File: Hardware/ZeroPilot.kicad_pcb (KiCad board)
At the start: 4 copper layers, 100 x 50 mm, 223 parts, among them J1 GH-6, J10 GH-4, J11 GH-3, J12 GH-4, J13 GH-2, J14 GH-4, J15 GH-4, J16 GH-4, J17 GH-4, J18 GH-6, J19 GH-6, J2 GH-6, J20 GH-6, J21 GH-6, J22 GH-6, J23 GH-6, J3 GH-6, J4 GH-6, J5 GH-6, J6 GH-6, J7 SPOX-2, J8 Micro_SD_Card, J9 USB_MICRO_B, Q1 Q_PMOS_DGS, Q2 Q_NMOS_GSD, U1 TPS54308, U10 STM32F030RCT6, U11 M24C64-WDW6TP, U12 ICM-20602, U13 MS5637-02BA03, U14 FT4232H, U2 TPS54308DDCT, U8 MCP1826S-3302E/DB, U9 STM32F765ZGT6, Y1 32.768kHz, Y2 8MHz, Y3 32.768kHz, Y4 8MHz, Y5 Crystal_GND24

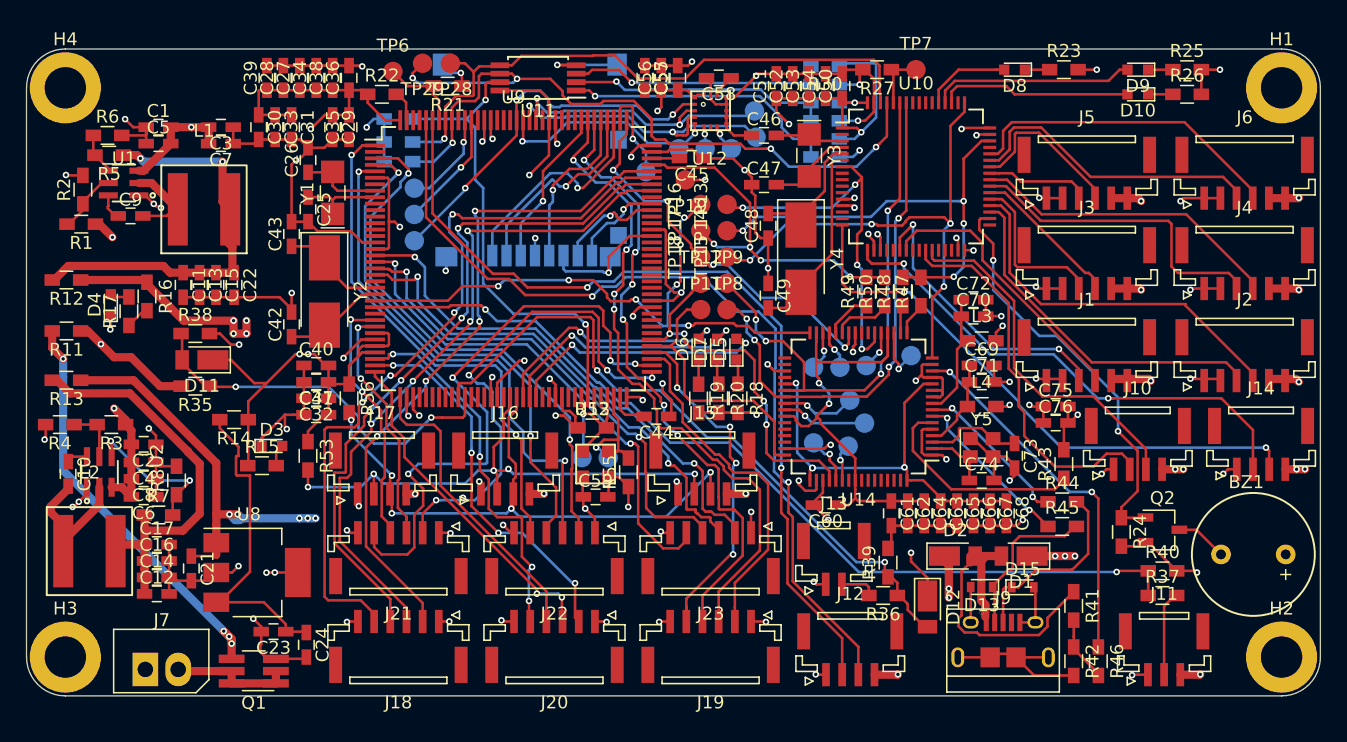
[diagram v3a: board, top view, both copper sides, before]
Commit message: Updated Footprints
Updated the footprints to 5.1, added 3D models to all components.
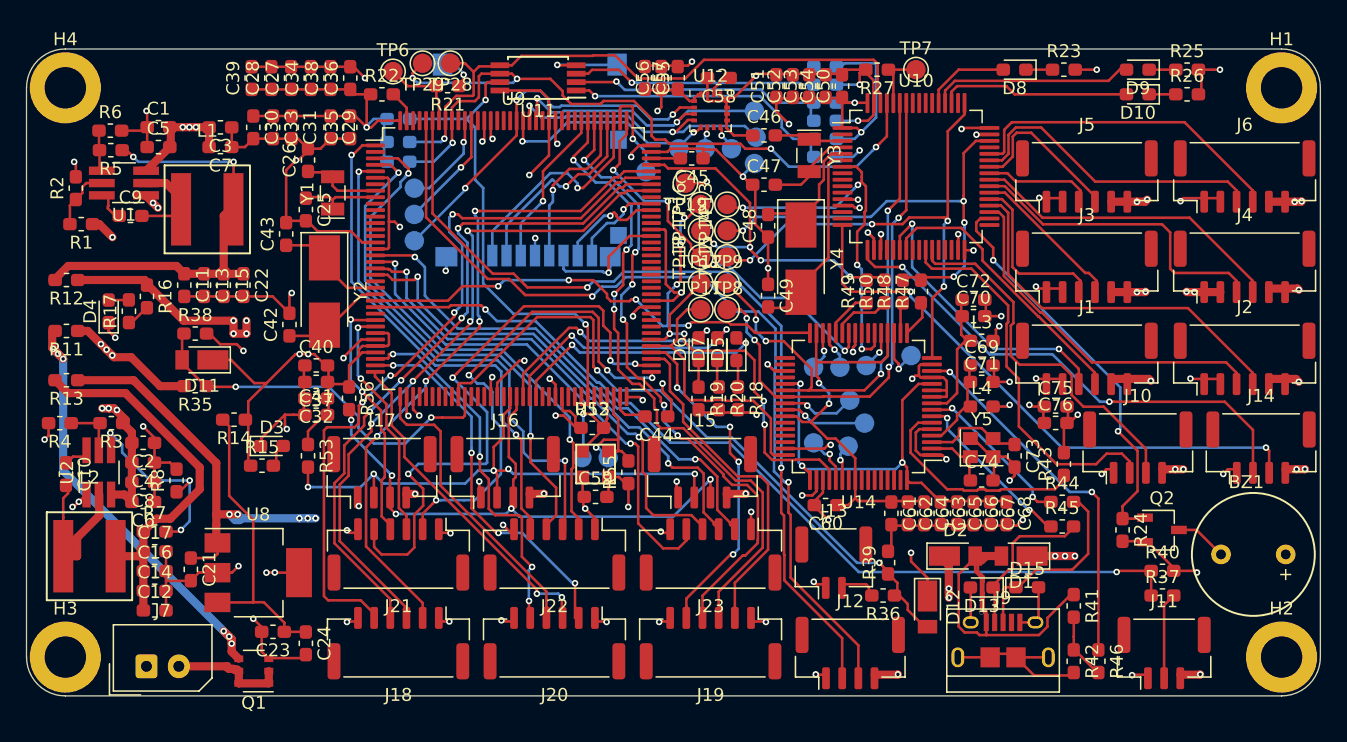
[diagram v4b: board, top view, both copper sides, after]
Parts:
- added TP10: GND_TST, TestPoint:TestPoint_Pad_D1.5mm, B.Cu at (106.3, 108.9)
- C1, C10, C11, C12, C13, C14, C15, C16, C17, C2, C21, C22, C23, C24, C25, C26, C27, C28, C29, C3, C30, C31, C32, C33, C34, C35, C36, C37, C38, C39, C4, C40, C41, C42, C43, C44, C45, C46, C47, C48, C49, C5, C50, C51, C52, C53, C54, C55, C56, C57, C58, C59, C6, C60, C61, C62, C63, C64, C65, C66, C67, C68, C69, C7, C70, C71, C72, C73, C74, C75, C76, C8, C9: footprint Capacitors_SMD:C_0603_HandSoldering -> Capacitor_SMD:C_0603_1608Metric_Pad1.05x0.95mm_HandSolder
- D1, D11, D12, D2: footprint Diodes_SMD:D_PowerDI-123 -> Diode_SMD:D_PowerDI-123
- D10, D3, D4, D5, D6, D7, D8, D9: footprint LEDs:LED_0603 -> LED_SMD:LED_0603_1608Metric_Pad1.05x0.95mm_HandSolder
- D13, D15: footprint Diodes_SMD:D_0603 -> Diode_SMD:D_0603_1608Metric_Pad1.05x0.95mm_HandSolder
- H1, H2, H3, H4: footprint Mounting_Holes:MountingHole_3.2mm_M3_ISO14580_Pad -> MountingHole:MountingHole_3.2mm_M3_ISO14580_Pad
- J1, J18, J19, J2, J20, J21, J22, J23, J3, J4, J5, J6: footprint Connectors_JST:JST_GH_BM06B-GHS-TBT_06x1.25mm_Straight -> Connector_JST:JST_GH_BM06B-GHS-TBT_1x06-1MP_P1.25mm_Vertical
- J10, J12, J14, J15, J16, J17: footprint Connectors_JST:JST_GH_BM04B-GHS-TBT_04x1.25mm_Straight -> Connector_JST:JST_GH_BM04B-GHS-TBT_1x04-1MP_P1.25mm_Vertical
- J11: footprint Connectors_JST:JST_GH_BM03B-GHS-TBT_03x1.25mm_Straight -> Connector_JST:JST_GH_BM03B-GHS-TBT_1x03-1MP_P1.25mm_Vertical
- J13: footprint Connectors_JST:JST_GH_BM02B-GHS-TBT_02x1.25mm_Straight -> Connector_JST:JST_GH_BM02B-GHS-TBT_1x02-1MP_P1.25mm_Vertical
- J7: footprint Connectors_Molex:Molex_SPOX-5267_22-03-5025_02x2.54mm_Straight -> Connector_Molex:Molex_SPOX_5267-02A_1x02_P2.50mm_Vertical
- L3, L4: footprint Inductors_SMD:L_0603_HandSoldering -> Inductor_SMD:L_0603_1608Metric_Pad1.05x0.95mm_HandSolder
- Q1: footprint WARG:TSOT-23-6_MK06A_HandSoldering -> WARG-kicad:IRF5806
- Q2: footprint TO_SOT_Packages_SMD:TSOT-23 -> Package_TO_SOT_SMD:TSOT-23
- R1, R11, R12, R13, R14, R15, R16, R17, R18, R19, R2, R20, R21, R22, R23, R24, R25, R26, R27, R28, R29, R3, R30, R31, R32, R33, R34, R35, R36, R37, R38, R39, R4, R40, R41, R42, R43, R44, R45, R46, R47, R48, R49, R5, R50, R51, R52, R53, R54, R55, R56, R6, R7, R8: footprint Resistors_SMD:R_0603_HandSoldering -> Resistor_SMD:R_0603_1608Metric_Pad1.05x0.95mm_HandSolder
- TP1, TP11, TP12, TP13, TP14, TP15, TP16, TP17, TP18, TP19, TP2, TP20, TP21, TP22, TP23, TP24, TP25, TP26, TP27, TP28, TP29, TP3, TP30, TP31, TP32, TP33, TP34, TP35, TP4, TP5, TP6, TP7, TP8, TP9: footprint Measurement_Points:Measurement_Point_Round-SMD-Pad_Small -> TestPoint:TestPoint_Pad_D1.5mm
- U1, U2: footprint WARG:TPS54308DDCT -> Package_TO_SOT_SMD:TSOT-23-6_HandSoldering
- U10, U14: footprint Housings_QFP:LQFP-64_10x10mm_Pitch0.5mm -> Package_QFP:LQFP-64_10x10mm_P0.5mm
- U11: footprint Housings_SSOP:TSSOP-8_4.4x3mm_Pitch0.65mm -> Package_SO:TSSOP-8_4.4x3mm_P0.65mm
- U12: footprint WARG:ICM-20602 -> Package_LGA:LGA-16_3x3mm_P0.5mm
- U13: footprint WARG:MS5637-02BA03 -> WARG-kicad:MS5637-02BA03
- U8: footprint TO_SOT_Packages_SMD:SOT-223 -> Package_TO_SOT_SMD:SOT-223
- U9: footprint Housings_QFP:LQFP-144_20x20mm_Pitch0.5mm -> Package_QFP:LQFP-144_20x20mm_P0.5mm
- Y1, Y3: footprint Crystals:Crystal_SMD_MicroCrystal_CC7V-T1A-2pin_3.2x1.5mm_HandSoldering -> Crystal:Crystal_SMD_MicroCrystal_CC7V-T1A-2Pin_3.2x1.5mm
- Y2, Y4: footprint Crystals:Crystal_SMD_5032-2pin_5.0x3.2mm_HandSoldering -> Crystal:Crystal_SMD_5032-2Pin_5.0x3.2mm_HandSoldering
- Y5: footprint Crystals:Crystal_SMD_2520-4pin_2.5x2.0mm -> Crystal:Crystal_SMD_2520-4Pin_2.5x2.0mm
- moved R7 1.32 mm to (59.9, 137.3)
- moved C12 1.29 mm to (59.9, 143.4)
- moved C39 1.18 mm to (67.4, 102.2)
- moved C14 1.04 mm to (59.9, 141.9)
- moved C28 0.93 mm to (68.9, 102.2)
- moved C16 0.79 mm to (59.9, 140.3)
- moved C22 0.72 mm to (66.8, 118.2)
- moved C27 0.67 mm to (70.4, 102.2)
- moved C15 0.60 mm to (65.2, 118.2)
- moved R2 0.56 mm to (53.8, 110.8)
- moved C17 0.55 mm to (59.9, 138.8)
- moved D4 0.55 mm to (56.4, 120.3)
- moved R6 0.43 mm to (56.5, 106.3)
- moved C30 0.42 mm to (67.5, 106.1)
- moved C34 0.42 mm to (72.0, 102.2)
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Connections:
- J9 pad 4: (no net) -> Net-(J9-Pad4)
- U10 pad 10: (no net) -> Net-(U10-Pad10)
- U10 pad 11: (no net) -> Net-(U10-Pad11)
- U10 pad 14: (no net) -> Net-(U10-Pad14)
- U10 pad 15: (no net) -> Net-(U10-Pad15)
- U10 pad 2: (no net) -> Net-(U10-Pad2)
- U10 pad 20: (no net) -> Net-(U10-Pad20)
- U10 pad 21: (no net) -> Net-(U10-Pad21)
- U10 pad 24: (no net) -> Net-(U10-Pad24)
- U10 pad 25: (no net) -> Net-(U10-Pad25)
- U10 pad 28: (no net) -> Net-(U10-Pad28)
- U10 pad 29: (no net) -> Net-(U10-Pad29)
- U10 pad 30: (no net) -> Net-(U10-Pad30)
- U10 pad 33: (no net) -> Net-(U10-Pad33)
- U10 pad 45: (no net) -> Net-(U10-Pad45)
- U10 pad 50: (no net) -> Net-(U10-Pad50)
- U10 pad 54: (no net) -> Net-(U10-Pad54)
- U10 pad 55: (no net) -> Net-(U10-Pad55)
- U10 pad 56: (no net) -> Net-(U10-Pad56)
- U10 pad 57: (no net) -> Net-(U10-Pad57)
- U10 pad 8: (no net) -> Net-(U10-Pad8)
- U10 pad 9: (no net) -> Net-(U10-Pad9)
- U12 pad 7: (no net) -> Net-(U12-Pad7)
- U14 pad 23: (no net) -> Net-(U14-Pad23)
- U14 pad 24: (no net) -> Net-(U14-Pad24)
- U14 pad 33: (no net) -> Net-(U14-Pad33)
- U14 pad 34: (no net) -> Net-(U14-Pad34)
- U14 pad 36: (no net) -> Net-(U14-Pad36)
- U14 pad 43: (no net) -> Net-(U14-Pad43)
- U14 pad 44: (no net) -> Net-(U14-Pad44)
- U14 pad 45: (no net) -> Net-(U14-Pad45)
- U14 pad 46: (no net) -> Net-(U14-Pad46)
- U14 pad 55: (no net) -> Net-(U14-Pad55)
- U14 pad 57: (no net) -> Net-(U14-Pad57)
- U14 pad 58: (no net) -> Net-(U14-Pad58)
- U14 pad 59: (no net) -> Net-(U14-Pad59)
- U14 pad 60: (no net) -> Net-(U14-Pad60)
- U14 pad 61: (no net) -> Net-(U14-Pad61)
- U14 pad 62: (no net) -> Net-(U14-Pad62)
- U14 pad 63: (no net) -> Net-(U14-Pad63)
- U9 pad 10: (no net) -> Net-(U9-Pad10)
- U9 pad 100: (no net) -> Net-(U9-Pad100)
- U9 pad 11: (no net) -> Net-(U9-Pad11)
- U9 pad 117: (no net) -> Net-(U9-Pad117)
- U9 pad 118: (no net) -> Net-(U9-Pad118)
- U9 pad 119: (no net) -> Net-(U9-Pad119)
- U9 pad 12: (no net) -> Net-(U9-Pad12)
- U9 pad 122: (no net) -> Net-(U9-Pad122)
- U9 pad 127: (no net) -> Net-(U9-Pad127)
- U9 pad 128: (no net) -> Net-(U9-Pad128)
- U9 pad 129: (no net) -> Net-(U9-Pad129)
- U9 pad 13: (no net) -> Net-(U9-Pad13)
- U9 pad 132: (no net) -> Net-(U9-Pad132)
- U9 pad 135: (no net) -> Net-(U9-Pad135)
- U9 pad 14: (no net) -> Net-(U9-Pad14)
- U9 pad 141: (no net) -> Net-(U9-Pad141)
- U9 pad 142: (no net) -> Net-(U9-Pad142)
- U9 pad 15: (no net) -> Net-(U9-Pad15)
- U9 pad 2: (no net) -> Net-(U9-Pad2)
- U9 pad 22: (no net) -> Net-(U9-Pad22)
- U9 pad 27: (no net) -> Net-(U9-Pad27)
- U9 pad 40: (no net) -> Net-(U9-Pad40)
- U9 pad 41: (no net) -> Net-(U9-Pad41)
- U9 pad 42: (no net) -> Net-(U9-Pad42)
- U9 pad 43: (no net) -> Net-(U9-Pad43)
- U9 pad 44: (no net) -> Net-(U9-Pad44)
- U9 pad 45: (no net) -> Net-(U9-Pad45)
- U9 pad 48: (no net) -> Net-(U9-Pad48)
- U9 pad 49: (no net) -> Net-(U9-Pad49)
- U9 pad 50: (no net) -> Net-(U9-Pad50)
- U9 pad 53: (no net) -> Net-(U9-Pad53)
- U9 pad 59: (no net) -> Net-(U9-Pad59)
- U9 pad 60: (no net) -> Net-(U9-Pad60)
- U9 pad 63: (no net) -> Net-(U9-Pad63)
- U9 pad 64: (no net) -> Net-(U9-Pad64)
- U9 pad 65: (no net) -> Net-(U9-Pad65)
- U9 pad 67: (no net) -> Net-(U9-Pad67)
- U9 pad 68: (no net) -> Net-(U9-Pad68)
- U9 pad 7: (no net) -> Net-(U9-Pad7)
- U9 pad 79: (no net) -> Net-(U9-Pad79)
- U9 pad 80: (no net) -> Net-(U9-Pad80)
- U9 pad 81: (no net) -> Net-(U9-Pad81)
- U9 pad 82: (no net) -> Net-(U9-Pad82)
- U9 pad 85: (no net) -> Net-(U9-Pad85)
- U9 pad 86: (no net) -> Net-(U9-Pad86)
- U9 pad 87: (no net) -> Net-(U9-Pad87)
- U9 pad 88: (no net) -> Net-(U9-Pad88)
- U9 pad 89: (no net) -> Net-(U9-Pad89)
- U9 pad 90: (no net) -> Net-(U9-Pad90)
- U9 pad 91: (no net) -> Net-(U9-Pad91)
- U9 pad 92: (no net) -> Net-(U9-Pad92)
- U9 pad 93: (no net) -> Net-(U9-Pad93)
- U9 pad 96: (no net) -> Net-(U9-Pad96)
- U9 pad 97: (no net) -> Net-(U9-Pad97)
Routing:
- net GND: track 309.8 -> 322.0 mm, vias 77 -> 78
- net /5V_USB: track 23.8 -> 30.8 mm
- net /POWER/INT_FB: track 11.8 -> 16.2 mm, vias 2 -> 3
- net /POWER/3V3_JMP: track 25.4 -> 23.4 mm
- net /POWER/6V_EXT_JMP: track 31.8 -> 33.4 mm
- net /VBATT: track 29.3 -> 30.8 mm, vias 4 -> 10
- net /POWER/EXT_SW: track 6.76 -> 8.27 mm
- net /POWER/5V_INT_JMP: track 31.3 -> 29.9 mm
- net /POWER/VBATT_JMP: track 32.3 -> 33.6 mm, vias 4 -> 6
- net /6V_EXT: track 37.3 -> 38.5 mm, vias 17 -> 20
- net Net-(C63-Pad1): track 33.5 -> 34.7 mm, vias 4 -> 3
- net /SAFETY_DBG_RX: track 42.5 -> 41.4 mm
- net /3V3: track 177.4 -> 178.5 mm, vias 28 -> 27
- net /RX4: track 48.1 -> 49.2 mm
- net /MISO1: track 23.2 -> 22.2 mm
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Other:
- net class Default: clearance 0.0889 -> 0.127
- rule trace_clearance: 0.0889 -> 0.127

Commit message: HW Bootcamp for Zeropilot R1
Changed the board to R1.
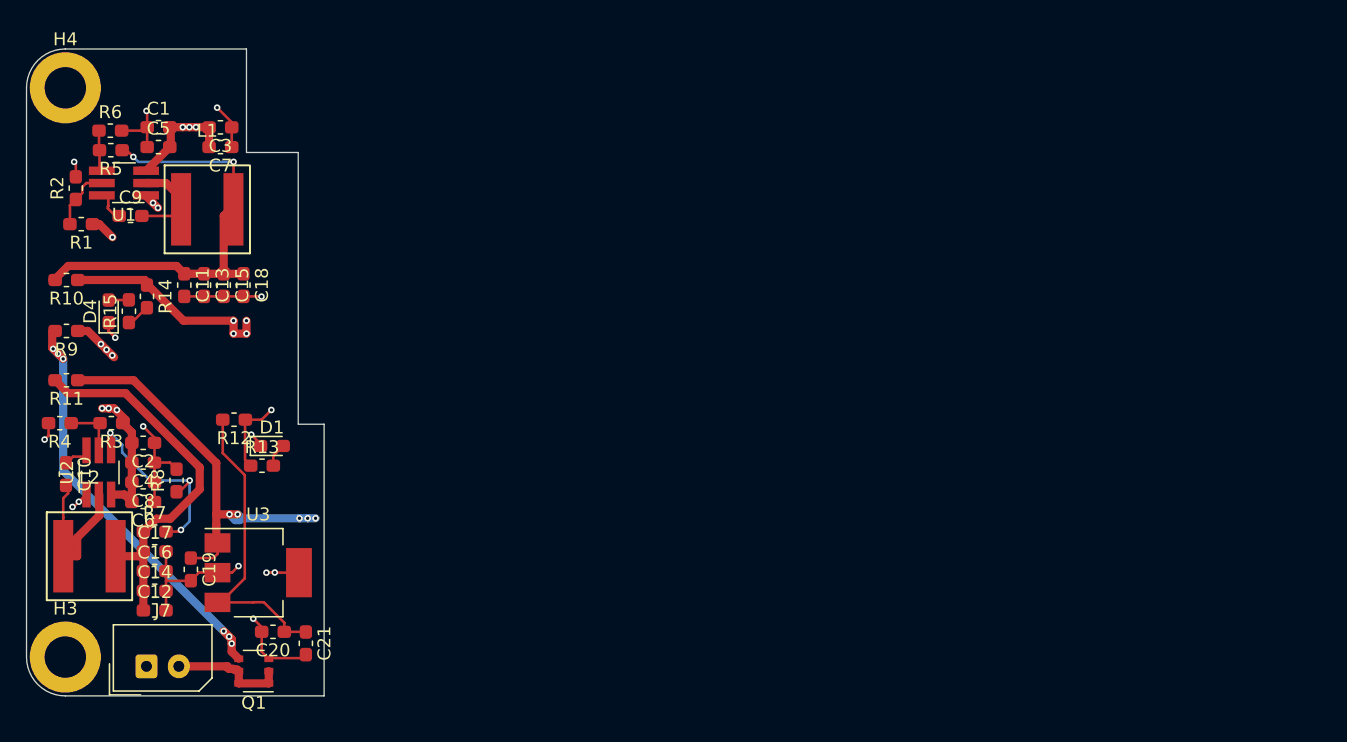
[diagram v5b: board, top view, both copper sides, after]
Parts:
- removed BZ1: Buzzer, WARG:AI-1027-TWT-3V-R
- removed C25, C26, C46, C47: 14pF, Capacitor_SMD:C_0603_1608Metric_Pad1.05x0.95mm_HandSolder
- removed C27, C28, C29, C30, C31, C32, C33, C34, C36, C37, C38, C39, C50, C51, C56, C58, C59, C60, C61, C62, C63, C64, C65, C66, C67, C69, C70, C76: 100nF, Capacitor_SMD:C_0603_1608Metric_Pad1.05x0.95mm_HandSolder
- removed C35, C40, C54: 1uF, Capacitor_SMD:C_0603_1608Metric_Pad1.05x0.95mm_HandSolder
- removed C41, C52, C68, C71, C72, C75: 4.7uF, Capacitor_SMD:C_0603_1608Metric_Pad1.05x0.95mm_HandSolder
- removed C42, C43, C48, C49: 7pF, Capacitor_SMD:C_0603_1608Metric_Pad1.05x0.95mm_HandSolder
- removed C44, C45, C57: 2.2uF, Capacitor_SMD:C_0603_1608Metric_Pad1.05x0.95mm_HandSolder
- removed C53, C55: 10nF, Capacitor_SMD:C_0603_1608Metric_Pad1.05x0.95mm_HandSolder
- removed C73, C74: 8pF, Capacitor_SMD:C_0603_1608Metric_Pad1.05x0.95mm_HandSolder
- removed the D1 at (126.9, 139.2)
- removed D10, D5, D6, D7, D8, D9: LED, LED_SMD:LED_0603_1608Metric_Pad1.05x0.95mm_HandSolder
- removed D11, D12, D2: D, Diode_SMD:D_PowerDI-123
- removed D13, D15: TVS, Diode_SMD:D_0603_1608Metric_Pad1.05x0.95mm_HandSolder
- removed H1, H2: MountingHole_M3, MountingHole:MountingHole_3.2mm_M3_ISO14580_Pad
- removed J1, J18, J19, J2, J20, J21, J22, J23, J3, J4, J5, J6: GH-6, Connector_JST:JST_GH_BM06B-GHS-TBT_1x06-1MP_P1.25mm_Vertical
- removed J10, J12, J14, J15, J16, J17: GH-4, Connector_JST:JST_GH_BM04B-GHS-TBT_1x04-1MP_P1.25mm_Vertical
- removed J11: GH-3, Connector_JST:JST_GH_BM03B-GHS-TBT_1x03-1MP_P1.25mm_Vertical
- removed J13: GH-2, Connector_JST:JST_GH_BM02B-GHS-TBT_1x02-1MP_P1.25mm_Vertical
- removed J8: Micro_SD_Card, WARG:micro_sd
- removed J9: USB_MICRO_B, WARG:USB_Micro-B_10118194-0001LF
- removed L3, L4: 600R, Inductor_SMD:L_0603_1608Metric_Pad1.05x0.95mm_HandSolder
- removed Q2: Q_NMOS_GSD, Package_TO_SOT_SMD:TSOT-23
- removed R18, R19, R20, R23, R25, R26: 100, Resistor_SMD:R_0603_1608Metric_Pad1.05x0.95mm_HandSolder
- removed R21, R27, R29, R31, R33, R34, R42, R51, R52, R53, R54, R55, R56: 10K, Resistor_SMD:R_0603_1608Metric_Pad1.05x0.95mm_HandSolder
- removed R22, R28, R30, R32, R48, R49: 0, Resistor_SMD:R_0603_1608Metric_Pad1.05x0.95mm_HandSolder
- removed R24: 100K, Resistor_SMD:R_0603_1608Metric_Pad1.05x0.95mm_HandSolder
- removed R35, R36: 150K, Resistor_SMD:R_0603_1608Metric_Pad1.05x0.95mm_HandSolder
- removed R37: 11K, Resistor_SMD:R_0603_1608Metric_Pad1.05x0.95mm_HandSolder
- removed R38, R39, R40: 22K, Resistor_SMD:R_0603_1608Metric_Pad1.05x0.95mm_HandSolder
- removed R41: 4.7K, Resistor_SMD:R_0603_1608Metric_Pad1.05x0.95mm_HandSolder
- removed R43: 12K, Resistor_SMD:R_0603_1608Metric_Pad1.05x0.95mm_HandSolder
- removed R44, R45: 10, Resistor_SMD:R_0603_1608Metric_Pad1.05x0.95mm_HandSolder
- removed R46: 1K, Resistor_SMD:R_0603_1608Metric_Pad1.05x0.95mm_HandSolder
- removed R47, R50: 220, Resistor_SMD:R_0603_1608Metric_Pad1.05x0.95mm_HandSolder
- removed TP1, TP2, TP28, TP29, TP3, TP30, TP31, TP32, TP33, TP34, TP35, TP4, TP5, TP6, TP7: TEST, TestPoint:TestPoint_Pad_D1.5mm
- removed TP10, TP19: GND_TST, TestPoint:TestPoint_Pad_D1.5mm
- removed TP11: TXP_TST, TestPoint:TestPoint_Pad_D1.5mm
- removed TP12: RXP_TST, TestPoint:TestPoint_Pad_D1.5mm
- removed TP13: NRSTS_TST, TestPoint:TestPoint_Pad_D1.5mm
- removed TP14: SWIOS_TST, TestPoint:TestPoint_Pad_D1.5mm
- removed TP15: SCLKS_TST, TestPoint:TestPoint_Pad_D1.5mm
- removed TP16: NRSTP_TST, TestPoint:TestPoint_Pad_D1.5mm
- removed TP17: SWIOP_TST, TestPoint:TestPoint_Pad_D1.5mm
- removed TP18: SCLKP_TST, TestPoint:TestPoint_Pad_D1.5mm
- removed TP20: TDO1_TST, TestPoint:TestPoint_Pad_D1.5mm
- removed TP21: TMS1_TST, TestPoint:TestPoint_Pad_D1.5mm
- removed TP22: TDO2_TST, TestPoint:TestPoint_Pad_D1.5mm
- removed TP23: TMS2_TST, TestPoint:TestPoint_Pad_D1.5mm
- removed TP24: UART1_RTS_TST, TestPoint:TestPoint_Pad_D1.5mm
- removed TP25: UART1_CTS_TST, TestPoint:TestPoint_Pad_D1.5mm
- removed TP26: UART2_RTS_TST, TestPoint:TestPoint_Pad_D1.5mm
- removed TP27: UART2_CTS_TST, TestPoint:TestPoint_Pad_D1.5mm
- removed TP8: TXS_TST, TestPoint:TestPoint_Pad_D1.5mm
- removed TP9: RXS_TST, TestPoint:TestPoint_Pad_D1.5mm
- removed U10: STM32F030RCT6, Package_QFP:LQFP-64_10x10mm_P0.5mm
- removed U11: M24C64-WDW6TP, Package_SO:TSSOP-8_4.4x3mm_P0.65mm
- removed U12: ICM-20602, Package_LGA:LGA-16_3x3mm_P0.5mm
- removed U13: MS5637-02BA03, WARG-kicad:MS5637-02BA03
- removed U14: FT4232H, Package_QFP:LQFP-64_10x10mm_P0.5mm
- removed U9: STM32F765ZGT6, Package_QFP:LQFP-144_20x20mm_P0.5mm
- removed Y1, Y3: 32.768kHz, Crystal:Crystal_SMD_MicroCrystal_CC7V-T1A-2Pin_3.2x1.5mm
- removed Y2, Y4: 8MHz, Crystal:Crystal_SMD_5032-2Pin_5.0x3.2mm_HandSoldering
- removed Y5: Crystal_GND24, Crystal:Crystal_SMD_2520-4Pin_2.5x2.0mm
- H3, H4: value MountingHole_M3 -> MountingHole
- renumbered C22 to C18, C21 to C19, C23 to C20, C24 to C21, D3 to D1, R12 to R10, R13 to R11, R14 to R12, R15 to R13, R16 to R14, R17 to R15, R11 to R9, U8 to U3
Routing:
- net GND: track 322.0 -> 51.4 mm, vias 78 -> 16
- net /3V3: track 178.5 -> 6.12 mm, vias 27 -> 1
- net /AIRSPD_ADC: track 70.6 -> 0.00 mm, vias 2 -> 0
- net /ULTRA_SONIC_2: track 69.3 -> 0.00 mm, vias 2 -> 0
- net /ULTRA_SONIC_1: track 67.7 -> 0.00 mm, vias 2 -> 0
- net /SCL1: track 59.6 -> 0.00 mm, vias 5 -> 0
- net /CTS1: track 57.9 -> 0.00 mm, vias 4 -> 0
- net /RX1: track 53.1 -> 0.00 mm, vias 4 -> 0
- net /TX1: track 52.3 -> 0.00 mm, vias 4 -> 0
- net /RTS1: track 52.3 -> 0.00 mm, vias 4 -> 0
- net /V_ISENSE_ADC: track 52.2 -> 0.00 mm, vias 2 -> 0
- net /TX4: track 50.4 -> 0.00 mm, vias 4 -> 0
- net /RX4: track 49.2 -> 0.00 mm, vias 6 -> 0
- net /SDA1: track 47.8 -> 0.00 mm, vias 1 -> 0
- net /NRST_PILOT: track 47.1 -> 0.00 mm, vias 7 -> 0
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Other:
- board size 100 x 50 mm -> 23 x 50 mm
- board text removed: "I2C"
- board text removed: "SPI"
- board text removed: "UART"

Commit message: bootcamp
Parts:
- added C19: 47uF, Capacitor_SMD:CP_Elec_4x3, F.Cu at (62.8, 125.1)
- added C20: 100uF, Capacitor_SMD:CP_Elec_4x3, F.Cu at (76.7, 120.0)
- added L3: 5uH, Capacitor_SMD:CP_Elec_5x4.5, F.Cu at (74.1, 113.9)
- added U3: LT1507CS8-3.3, Package_TO_SOT_SMD:TSOT-23-8, F.Cu at (83.2, 113.7)
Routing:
- net /VBATT: track 24.7 -> 64.6 mm
- net /POWER/3V3_JMP: track 24.2 -> 44.5 mm
- net GND: track 51.4 -> 70.0 mm, vias 16 -> 17
- net Net-(C20-Pad2): track 0.00 -> 14.3 mm
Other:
- board size 23 x 50 mm -> 39.4 x 50 mm

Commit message: Revert "bootcamp"
This reverts commit e17f23a9567473d5c63a4d79c7567bac12ecac0d.
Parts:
- removed the C19 at (62.8, 125.1)
- removed the C20 at (76.7, 120.0)
- removed L3: 5uH, Capacitor_SMD:CP_Elec_5x4.5
- removed the U3 at (83.2, 113.7)
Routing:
- net /VBATT: track 64.6 -> 24.7 mm
- net /POWER/3V3_JMP: track 44.5 -> 24.2 mm
- net GND: track 70.0 -> 51.4 mm, vias 17 -> 16
- net Net-(C20-Pad2): track 14.3 -> 0.00 mm
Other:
- board size 39.4 x 50 mm -> 23 x 50 mm

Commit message: second run thru of bootcamp
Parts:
- added C19: 10uF, Capacitor_SMD:C_0805_2012Metric_Pad1.18x1.45mm_HandSolder, F.Cu at (69.5, 124.2)
- added C20: 100nF, Capacitor_SMD:C_0805_2012Metric_Pad1.18x1.45mm_HandSolder, F.Cu at (76.7, 114.5)
- added C21: 44uF, Capacitor_SMD:C_0805_2012Metric_Pad1.18x1.45mm_HandSolder, F.Cu at (71.6, 111.1)
- added L3: 3.9uH, Inductor_SMD:L_1812_4532Metric_Pad1.30x3.40mm_HandSolder, F.Cu at (75.9, 120.7)
- added U3: AP63203WU-7, Regulator:AP63203WU-7, F.Cu at (71.8, 112.9)
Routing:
- net /VBATT: track 24.7 -> 50.9 mm
- net /3V3: track 6.12 -> 30.8 mm
- net GND: track 51.4 -> 64.7 mm, vias 16 -> 17
- net Net-(C20-Pad2): track 0.00 -> 7.34 mm
- net Net-(C20-Pad1): track 0.00 -> 4.00 mm
- removed copper zone on PWR, net /3V3
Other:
- board size 23 x 50 mm -> 29.1 x 50 mm
